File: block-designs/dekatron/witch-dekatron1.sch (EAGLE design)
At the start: 17 parts, among them IC1 4002N, IC3 74HC160N, IC4 4511N

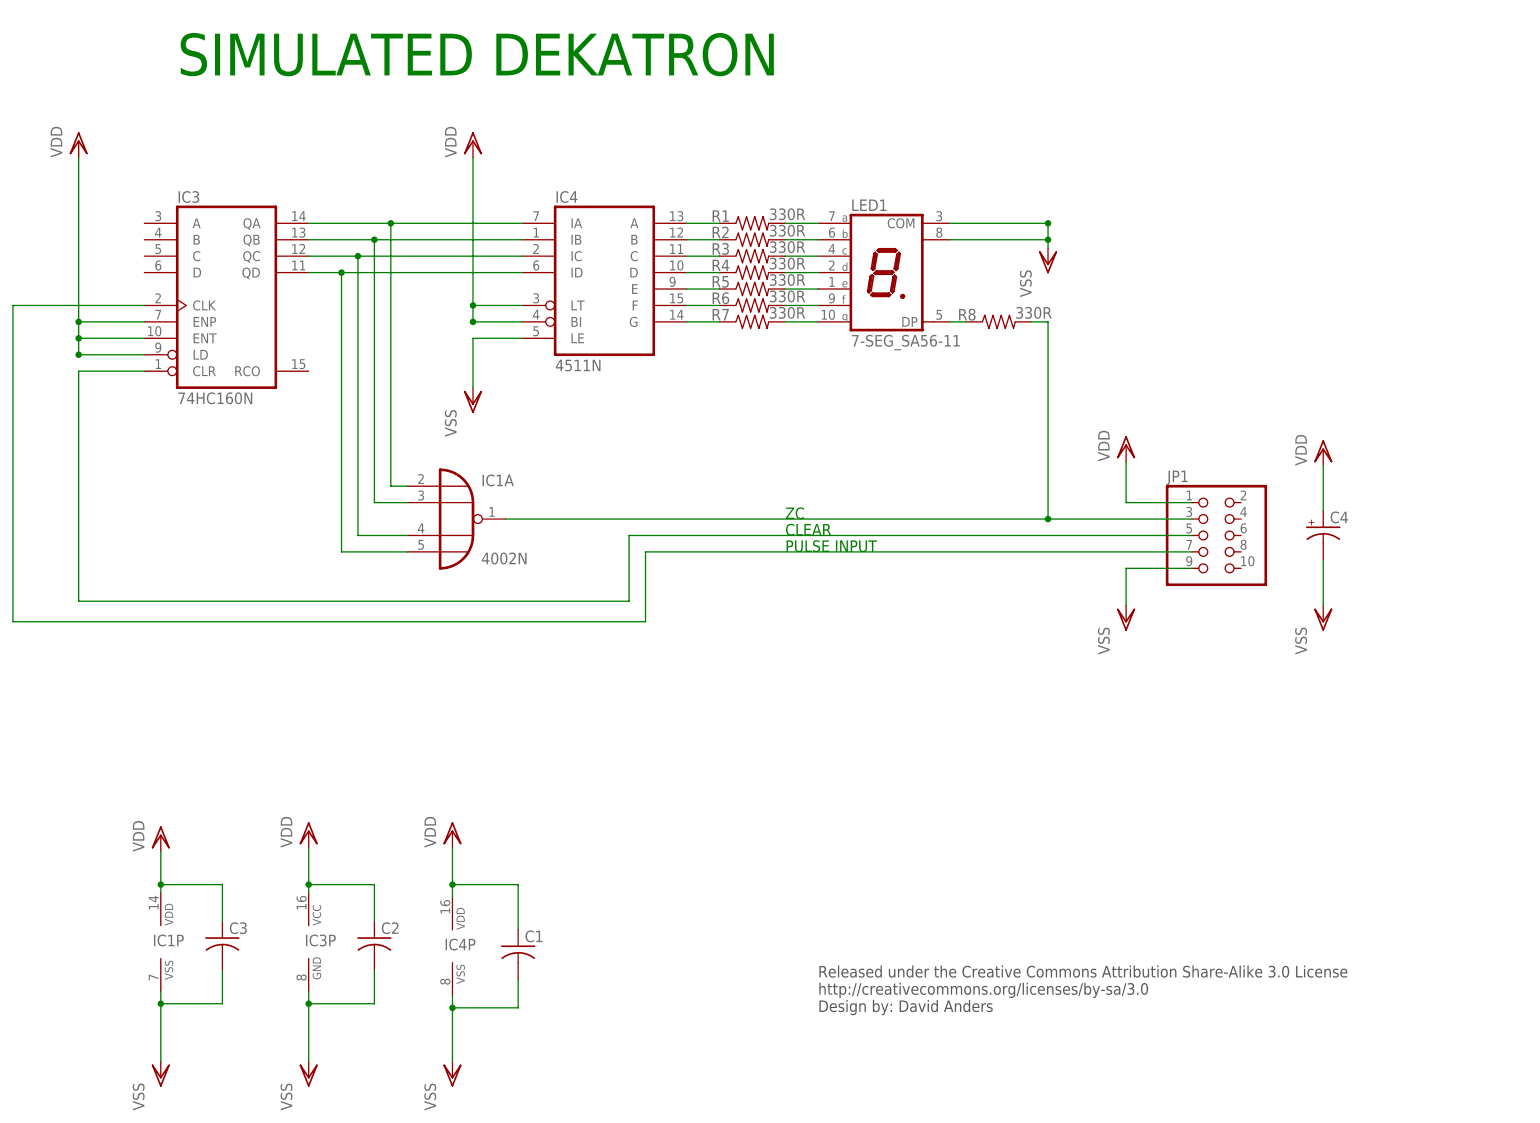
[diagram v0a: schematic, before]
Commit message: updated dekatron layout
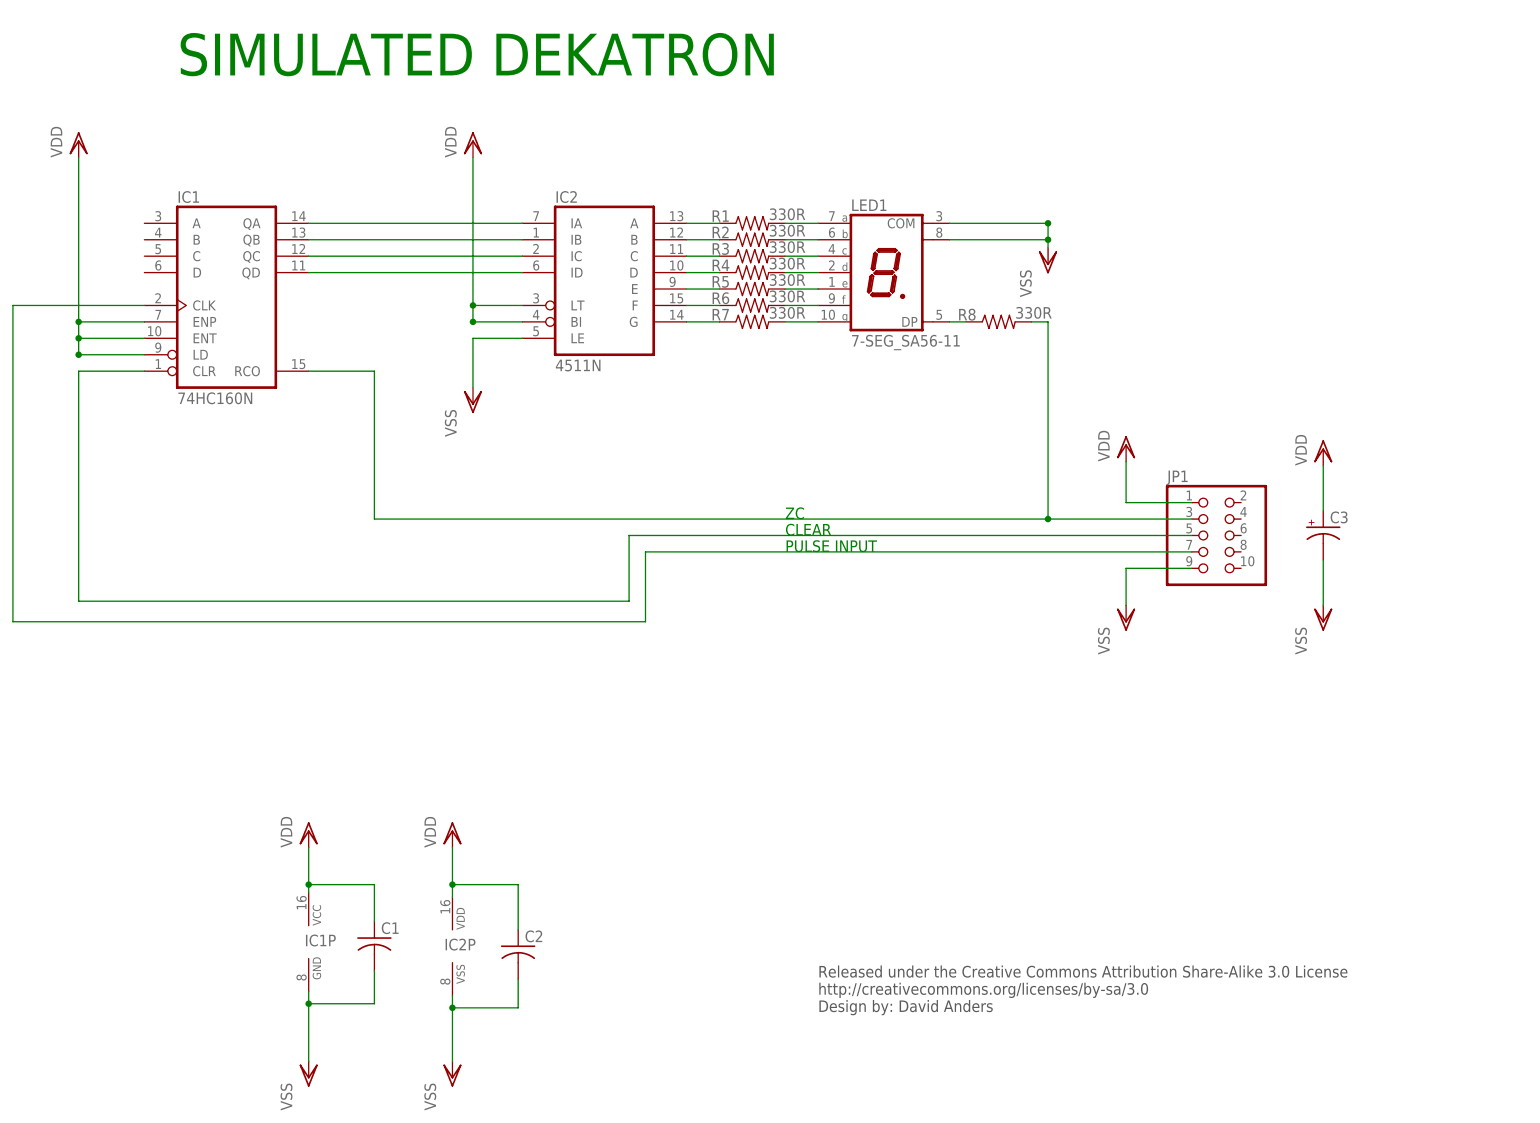
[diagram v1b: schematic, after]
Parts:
- removed C4: (no value), resistor:CPOL-USE2-5
- removed IC3: 74HC160N, 74xx-eu:74HC160N
- C3: device resistor:C-US025-025X050 -> resistor:CPOL-USE2-5
- IC1: value 4002N -> 74HC160N; device 40xx:4002N -> 74xx-eu:74HC160N
- renumbered IC4 to IC2
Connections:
- net N$1: now also IC1A.RCO; no longer IC1A.O
- net N$10: now also IC1A.QA; no longer IC1A.I0, IC3A.QA
- net N$11: now also IC1A.QB; no longer IC1A.I1, IC3A.QB
- net N$12: now also IC1A.QC; no longer IC1A.I2, IC3A.QC
- net N$13: now also IC1A.QD; no longer IC1A.I3, IC3A.QD
- net N$2: now also IC1A.CLR; no longer IC3A.CLR
- net N$25: now also IC1A.CLK; no longer IC3A.CLK
- net VDD: now also C3.+, IC1A.ENP, IC1A.ENT, IC1A.LD, IC1P.VCC; no longer C3.1, C4.+, IC1P.VDD, IC3A.ENP, IC3A.ENT, IC3A.LD, IC3P.VCC
- net VSS: now also C3.-, IC1P.GND; no longer C3.2, C4.-, IC1P.VSS, IC3P.GND
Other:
- moved on the sheet: C1, C2, IC1P
